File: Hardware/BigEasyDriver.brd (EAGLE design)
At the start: 36.8 x 30.5 mm, 56 parts, among them IC1 A4983ALT1, IC2 LM317L

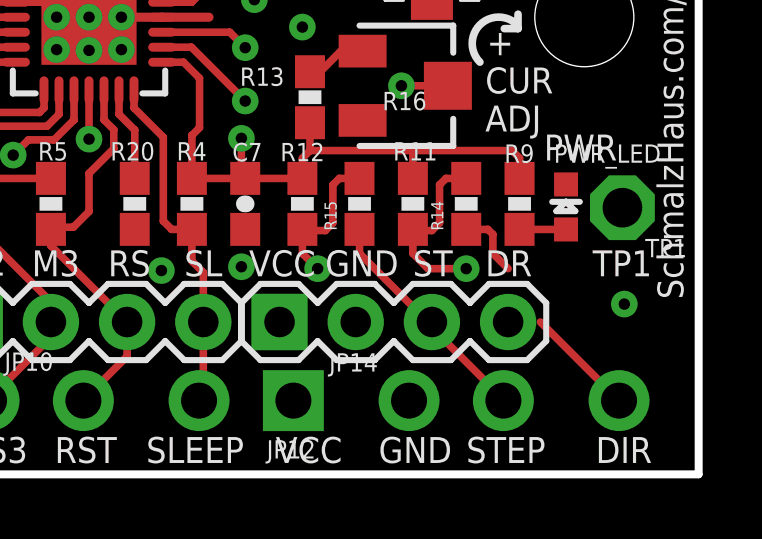
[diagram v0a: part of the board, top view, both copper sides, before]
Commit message: Updating part package w/ Sparkle IDs
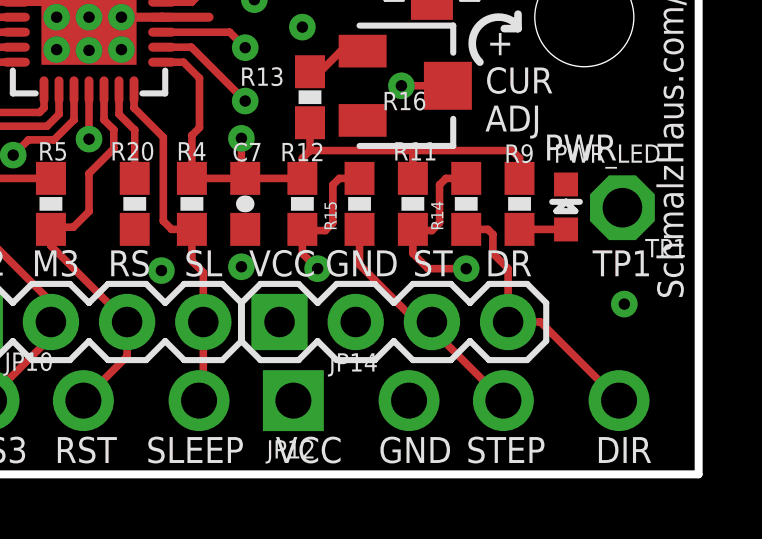
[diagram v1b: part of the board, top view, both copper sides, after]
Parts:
- C1, C10, C11, C2, C6, C7, C8, C9: device SparkFun:0603-CAP -> SparkFun-Capacitors:0603-CAP
- C14: device SparkFun:PANASONIC_D -> SparkFun-Capacitors:PANASONIC_D
- R1, R10, R11, R12, R13, R14, R15, R2, R20, R3, R4, R5, R6, R7, R8, R9: device SparkFun:0603-RES -> SparkFun-Resistors:0603-RES
- R18, R19: device SparkFun:R2010 -> SparkFun-Resistors:R2010
- moved FRAME1 77.1 mm to (-11.8, -11.4)
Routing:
- net DIR_IN: track 6.02 -> 8.87 mm
- net STEP_IN: track 7.45 -> 7.99 mm

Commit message: Adding 4 layer note to tDocu on board
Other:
- board text added: "Produced by SparkFun Electronics"
- board text added: "Revised by: Patrick Alberts/Toni Klopfenstein"
- board text added: "THIS IS A 4-LAYER BOARD."
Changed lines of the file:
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@@
 <?xml version="1.0" encoding="utf-8"?>
 <!DOCTYPE eagle SYSTEM "eagle.dtd">
-<eagle version="6.5.0">
+<eagle version="6.6.0">
 <drawing>
 <settings>
@@
 <setting verticaltext="up"/>
 </settings>
-<grid distance="0.05" unitdist="inch" unit="inch" style="lines" multiple="1" display="yes" altdistance="0.005" altunitdist="inch" altunit="inch"/>
+<grid distance="1" unitdist="mm" unit="mm" style="lines" multiple="1" display="yes" altdistance="0.1" altunitdist="mm" altunit="mm"/>
 <layers>
 <layer number="1" name="Top" color="4" fill="1" visible="yes" active="yes"/>
@@
 <layer number="17" name="Pads" color="2" fill="1" visible="yes" active="yes"/>
 <layer number="18" name="Vias" color="2" fill="1" visible="yes" active="yes"/>
-<layer number="19" name="Unrouted" color="11" fill="1" visible="yes" active="yes"/>
-<layer number="20" name="Dimension" color="6" fill="1" visible="yes" active="yes"/>
+<layer number="19" name="Unrouted" color="6" fill="1" visible="yes" active="yes"/>
+<layer number="20" name="Dimension" color="15" fill="1" visible="yes" active="yes"/>
 <layer number="21" name="tPlace" color="16" fill="1" visible="yes" active="yes"/>
 <layer number="22" name="bPlace" color="14" fill="1" visible="yes" active="yes"/>
@@
 <wire x1="30.353" y1="14.859" x2="30.8102" y2="14.859" width="0.254" layer="21"/>
 <wire x1="30.8102" y1="14.859" x2="30.8102" y2="15.3416" width="0.254" layer="21"/>
-<text x="-30.48" y="-16.51" size="1.778" layer="27" font="vector">Brian Schmalz: http://schmalzhaus.com/BigEasyDriver/index.html</text>
+<text x="0" y="-13.97" size="1.778" layer="27" font="vector">Brian Schmalz: http://schmalzhaus.com/BigEasyDriver/index.html</text>
 <wire x1="0.762" y1="1.397" x2="0.762" y2="3.683" width="0.254" layer="22"/>
 <wire x1="0.762" y1="3.683" x2="3.81" y2="3.683" width="0.254" layer="22"/>
@@
 <wire x1="28.956" y1="3.683" x2="35.56" y2="3.683" width="0.254" layer="22"/>
 <wire x1="35.56" y1="3.683" x2="35.56" y2="1.397" width="0.254" layer="22"/>
+<text x="0" y="-16.51" size="1.778" layer="51" font="vector" ratio="15">Revised by: Patrick Alberts/Toni Klopfenstein</text>
+<text x="0" y="-19.05" size="1.778" layer="51" font="vector" ratio="15">Produced by SparkFun Electronics</text>
+<text x="-6" y="33" size="2.54" layer="51" font="vector" ratio="15">THIS IS A 4-LAYER BOARD. </text>
 </plain>
 <attributes>

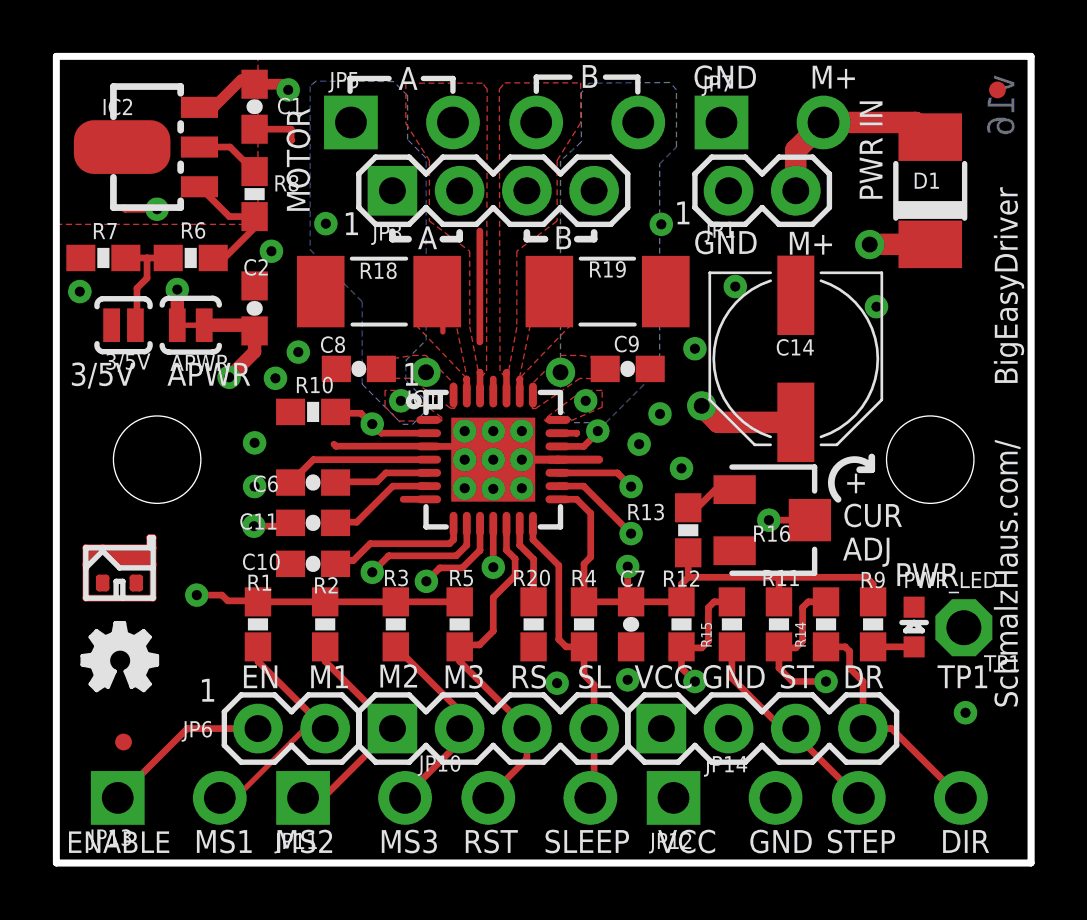
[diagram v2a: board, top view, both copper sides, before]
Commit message: changed fiducials to regulars
also deleted old panels in prep for new ones
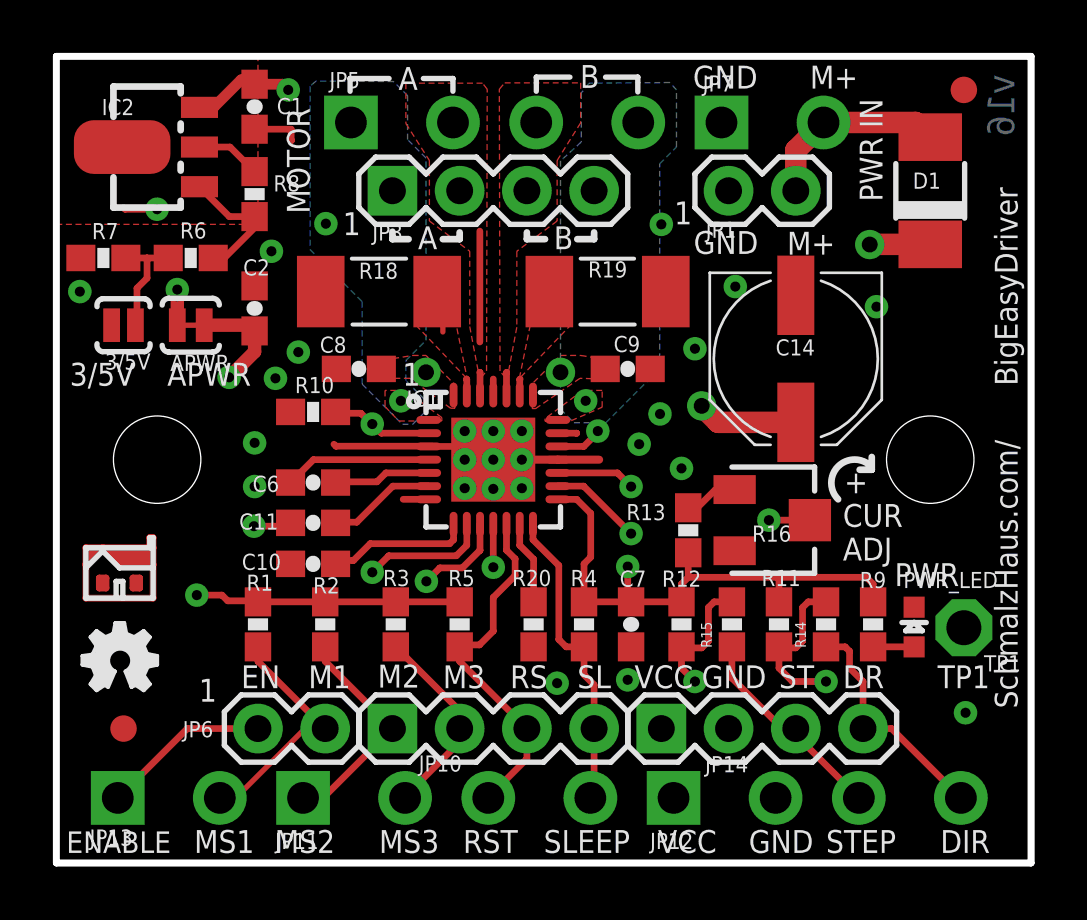
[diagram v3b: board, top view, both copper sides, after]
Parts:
- removed JP2, JP4: FIDUCIAL1X2.5, abes:FIDUCIAL-1X2.5
- added FID1, FID2: FIDUCIAL1X2, SparkFun-Aesthetics:FIDUCIAL-1X2

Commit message: Updating version number to show change in CAM job
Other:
- board text added: "v16a"
- board text removed: "v16"

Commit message: Updating IC to proper A4988 device
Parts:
- IC1: value A4983ALT1 -> A4988ALT1; device Testing:QFN-28-5MM_ALT1 -> SparkFun-PowerIC:QFN-28-5MM_ALT1
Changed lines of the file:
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@@
 <?xml version="1.0" encoding="utf-8"?>
 <!DOCTYPE eagle SYSTEM "eagle.dtd">
-<eagle version="7.1.0">
+<eagle version="7.2.0">
 <drawing>
 <settings>
@@
 <layer number="11" name="Route11" color="4" fill="7" visible="no" active="no"/>
 <layer number="56" name="wert" color="7" fill="1" visible="no" active="no"/>
+<layer number="57" name="tCAD" color="7" fill="1" visible="no" active="no"/>
+<layer number="59" name="tCarbon" color="7" fill="1" visible="no" active="no"/>
+<layer number="60" name="bCarbon" color="7" fill="1" visible="no" active="no"/>
+<layer number="90" name="Modules" color="5" fill="1" visible="no" active="no"/>
 <layer number="91" name="Nets" color="2" fill="1" visible="no" active="no"/>
 <layer number="92" name="Busses" color="1" fill="1" visible="no" active="no"/>
@@
 <layer number="97" name="Info" color="7" fill="1" visible="no" active="no"/>
 <layer number="98" name="Guide" color="6" fill="1" visible="no" active="no"/>
+<layer number="99" name="SpiceOrder" color="7" fill="1" visible="no" active="no"/>
 <layer number="100" name="Muster" color="7" fill="1" visible="no" active="no"/>
 <layer number="101" name="Patch_Top" color="12" fill="4" visible="no" active="no"/>
@@
 <layer number="108" name="tplace-old" color="10" fill="1" visible="no" active="yes"/>
 <layer number="109" name="ref-old" color="11" fill="1" visible="no" active="yes"/>
+<layer number="110" name="fp0" color="7" fill="1" visible="yes" active="yes"/>
+<layer number="111" name="LPC17xx" color="7" fill="1" visible="yes" active="yes"/>
+<layer number="112" name="tSilk" color="7" fill="1" visible="yes" active="yes"/>
+<layer number="113" name="IDFDebug" color="4" fill="1" visible="yes" active="yes"/>
 <layer number="116" name="Patch_BOT" color="9" fill="4" visible="no" active="no"/>
+<layer number="118" name="Rect_Pads" color="7" fill="1" visible="yes" active="yes"/>
 <layer number="121" name="_tsilk" color="14" fill="1" visible="no" active="yes"/>
 <layer number="122" name="_bsilk" color="14" fill="1" visible="no" active="yes"/>
+<layer number="123" name="tTestmark" color="7" fill="1" visible="yes" active="yes"/>
+<layer number="124" name="bTestmark" color="7" fill="1" visible="yes" active="yes"/>
 <layer number="125" name="_tNames" color="7" fill="1" visible="no" active="yes"/>
+<layer number="126" name="_bNames" color="7" fill="1" visible="yes" active="yes"/>
+<layer number="127" name="_tValues" color="7" fill="1" visible="yes" active="yes"/>
+<layer number="128" name="_bValues" color="7" fill="1" visible="yes" active="yes"/>
+<layer number="129" name="Mask" color="7" fill="1" visible="yes" active="yes"/>
+<layer number="131" name="tAdjust" color="7" fill="1" visible="yes" active="yes"/>
+<layer number="132" name="bAdjust" color="7" fill="1" visible="yes" active="yes"/>
 <layer number="144" name="DrillLegend" color="7" fill="1" visible="no" active="yes"/>
+<layer number="150" name="Notes" color="7" fill="1" visible="yes" active="yes"/>
 <layer number="151" name="HeatSink" color="7" fill="1" visible="no" active="no"/>
+<layer number="152" name="_bDocu" color="7" fill="1" visible="yes" active="yes"/>
+<layer number="153" name="FabDoc1" color="7" fill="1" visible="yes" active="yes"/>
+<layer number="154" name="FabDoc2" color="7" fill="1" visible="yes" active="yes"/>
+<layer number="155" name="FabDoc3" color="7" fill="1" visible="yes" active="yes"/>
 <layer number="199" name="Contour" color="7" fill="1" visible="no" active="yes"/>
 <layer number="200" name="200bmp" color="1" fill="10" visible="no" active="no"/>
@@
 <layer number="223" name="223bmp" color="24" fill="1" visible="no" active="no"/>
 <layer number="224" name="224bmp" color="25" fill="1" visible="no" active="no"/>
+<layer number="225" name="225bmp" color="7" fill="1" visible="yes" active="yes"/>
+<layer number="226" name="226bmp" color="7" fill="1" visible="yes" active="yes"/>
+<layer number="227" name="227bmp" color="7" fill="1" visible="yes" active="yes"/>
+<layer number="228" name="228bmp" color="7" fill="1" visible="yes" active="yes"/>
+<layer number="229" name="229bmp" color="7" fill="1" visible="yes" active="yes"/>
+<layer number="230" name="230bmp" color="7" fill="1" visible="yes" active="yes"/>
+<layer number="231" name="231bmp" color="7" fill="1" visible="yes" active="yes"/>
+<layer number="248" name="Housing" color="7" fill="1" visible="yes" active="yes"/>
+<layer number="249" name="Edge" color="7" fill="1" visible="yes" active="yes"/>
 <layer number="250" name="Descript" color="3" fill="1" visible="no" active="no"/>
 <layer number="251" name="SMDround" color="12" fill="11" visible="no" active="no"/>
 <layer number="254" name="cooling" color="7" fill="1" visible="no" active="no"/>
+<layer number="255" name="routoute" color="7" fill="1" visible="yes" active="yes"/>
 </layers>
 <board>
@@
 <attribute name="PROD_ID" value="RES-08354" x="20.828" y="21.59" size="1.778" layer="27" rot="R180" display="off"/>
 </element>
-<element name="IC1" library="Testing" package="QFN-28-5MM_ALT1" value="A4983ALT1" x="16.51" y="15.24" smashed="yes">
+<element name="IC1" library="SparkFun-PowerIC" package="QFN-28-5MM_ALT1" value="A4988ALT1" x="16.51" y="15.24" smashed="yes">
 <attribute name="NAME" x="13.2334" y="17.2466" size="0.6096" layer="25"/>
 <attribute name="VALUE" x="15.2146" y="18.4404" size="0.6096" layer="27"/>
+<attribute name="PROD_ID" value="IC-11483" x="16.51" y="15.24" size="1.778" layer="27" display="off"/>
 </element>
 <element name="R20" library="SparkFun-Resistors" package="0603-RES" value="20K" x="18.034" y="9.017" smashed="yes" rot="R270">
